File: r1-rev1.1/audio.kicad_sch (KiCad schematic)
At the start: 28 parts, among them J4 HP_3.5mm, J5 LO_3.5mm, Q6 AO3401A, Q7 AO3401A, U9 TLV320AIC3104

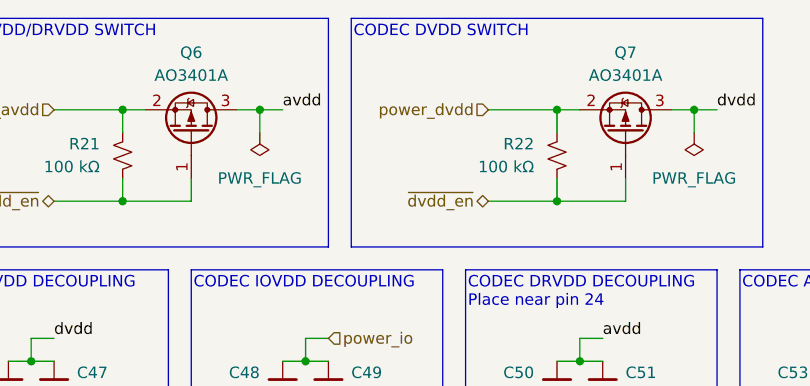
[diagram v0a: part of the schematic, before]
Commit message: Fix symbol library links & resync footprints from KiCAD libraries
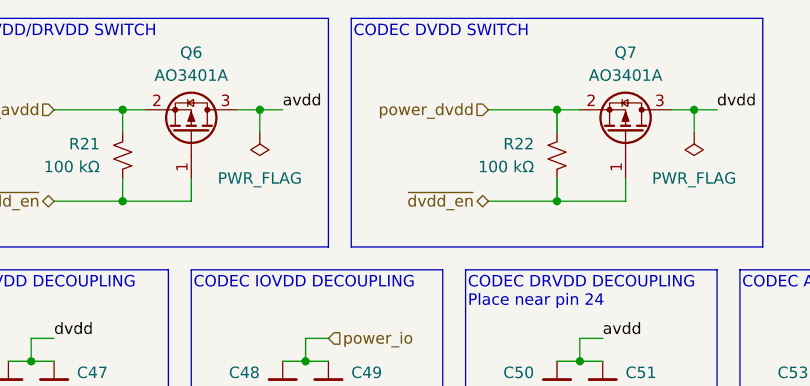
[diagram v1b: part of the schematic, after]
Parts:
- Q6, Q7: symbol Device:Q_PMOS_GSD -> Transistor_FET:Q_PMOS_GSD
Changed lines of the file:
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@@
 	)
 	(symbol
-		(lib_id "Device:Q_PMOS_GSD")
+		(lib_id "Transistor_FET:Q_PMOS_GSD")
 		(at 132.08 27.94 270)
 		(mirror x)
@@
 	)
 	(symbol
-		(lib_id "Device:Q_PMOS_GSD")
+		(lib_id "Transistor_FET:Q_PMOS_GSD")
 		(at 83.82 27.94 270)
 		(mirror x)

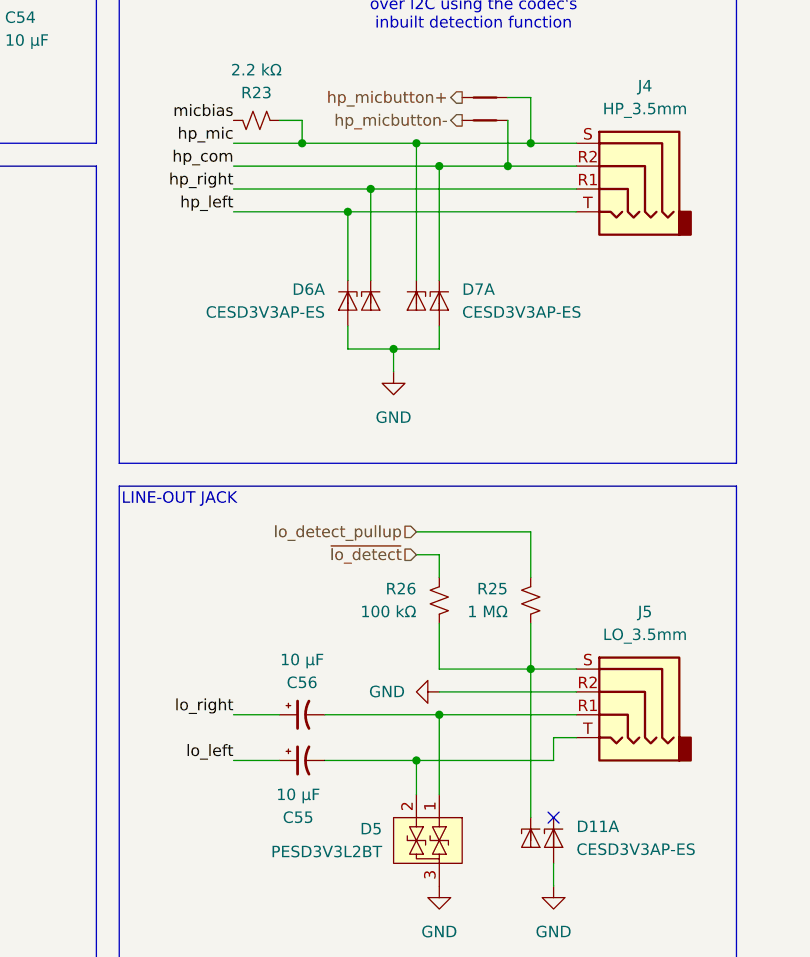
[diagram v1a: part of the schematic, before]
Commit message: Fix incorrect 3.5mm jack pinout
Document the R1-Rev1's wrong pinout properly and fix the pinout
in later revs so that jacks will work properly without needing
a custom adapter.

See Github issue: #12
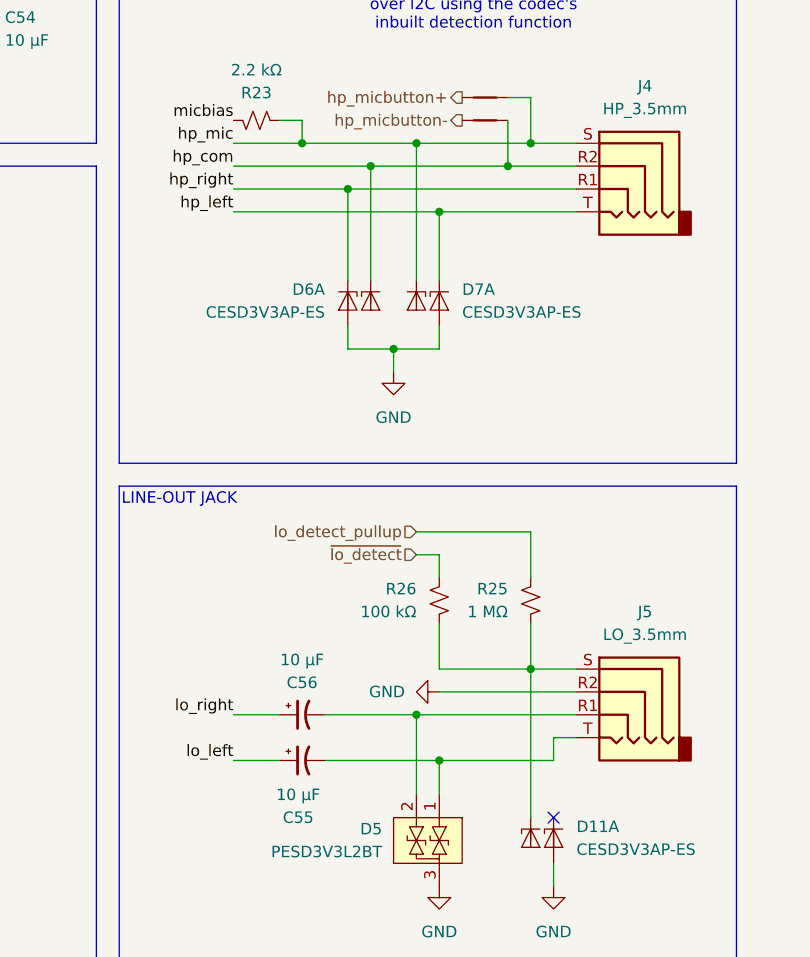
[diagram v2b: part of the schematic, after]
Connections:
- net hp_com: now also D6.2 (K2); no longer D7.1 (K1)
- net hp_left: now also D7.1 (K1); no longer D6.1 (K1)
- net hp_right: now also D6.1 (K1); no longer D6.2 (K2)
- net at C56.2, J5.R1: now also D5.2 (IO2); no longer D5.1 (IO1)
- net at C55.2, J5.T: now also D5.1 (IO1); no longer D5.2 (IO2)
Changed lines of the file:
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@@
+	)
+	(junction
+		(at 210.82 137.16)
+		(diameter 0)
+		(color 0 0 0 0)
 	)
 	(junction
@@
 	)
 	(junction
+		(at 210.82 76.2)
+		(diameter 0)
+		(color 0 0 0 0)
+	)
+	(junction
 		(at 139.7 25.4)
 		(diameter 0)
@@
 	)
 	(junction
+		(at 200.66 73.66)
+		(diameter 0)
+		(color 0 0 0 0)
+	)
+	(junction
 		(at 106.68 91.44)
 		(diameter 0)
@@
 	)
 	(junction
-		(at 210.82 71.12)
-		(diameter 0)
-		(color 0 0 0 0)
-	)
-	(junction
 		(at 134.62 147.32)
 		(diameter 0)
@@
 	)
 	(junction
+		(at 208.28 132.08)
+		(diameter 0)
+		(color 0 0 0 0)
+	)
+	(junction
 		(at 218.44 71.12)
 		(diameter 0)
@@
 	)
 	(junction
-		(at 200.66 76.2)
-		(diameter 0)
-		(color 0 0 0 0)
-	)
-	(junction
 		(at 205.74 91.44)
 		(diameter 0)
@@
 	)
 	(junction
-		(at 203.2 73.66)
-		(diameter 0)
-		(color 0 0 0 0)
-	)
-	(junction
 		(at 127 53.34)
 		(diameter 0)
@@
 	)
 	(junction
-		(at 208.28 137.16)
-		(diameter 0)
-		(color 0 0 0 0)
-	)
-	(junction
-		(at 210.82 132.08)
-		(diameter 0)
-		(color 0 0 0 0)
-	)
-	(junction
 		(at 101.6 157.48)
 		(diameter 0)
@@
 	(junction
 		(at 134.62 144.78)
+		(diameter 0)
+		(color 0 0 0 0)
+	)
+	(junction
+		(at 203.2 71.12)
 		(diameter 0)
 		(color 0 0 0 0)
@@
 	(wire
 		(pts
-			(xy 200.66 76.2) (xy 200.66 83.82)
-		)
-		(stroke
-			(width 0)
-			(type default)
-		)
-	)
-	(wire
-		(pts
 			(xy 106.68 154.94) (xy 106.68 157.48)
 		)
@@
 	(wire
 		(pts
-			(xy 208.28 137.16) (xy 223.52 137.16)
-		)
-		(stroke
-			(width 0)
-			(type default)
-		)
-	)
-	(wire
-		(pts
 			(xy 134.62 144.78) (xy 134.62 147.32)
 		)
@@
 	(wire
 		(pts
-			(xy 210.82 132.08) (xy 226.06 132.08)
+			(xy 198.12 132.08) (xy 208.28 132.08)
 		)
 		(stroke
@@
 	(wire
 		(pts
+			(xy 208.28 132.08) (xy 208.28 140.97)
+		)
+		(stroke
+			(width 0)
+			(type default)
+		)
+	)
+	(wire
+		(pts
 			(xy 134.62 104.14) (xy 134.62 109.22)
 		)
@@
 	(wire
 		(pts
-			(xy 203.2 73.66) (xy 203.2 83.82)
-		)
-		(stroke
-			(width 0)
-			(type default)
-		)
-	)
-	(wire
-		(pts
 			(xy 76.2 35.56) (xy 68.58 35.56)
 		)
@@
 	(wire
 		(pts
-			(xy 203.2 73.66) (xy 226.06 73.66)
-		)
-		(stroke
-			(width 0)
-			(type default)
-		)
-	)
-	(wire
-		(pts
-			(xy 200.66 76.2) (xy 226.06 76.2)
+			(xy 200.66 73.66) (xy 226.06 73.66)
+		)
+		(stroke
+			(width 0)
+			(type default)
+		)
+	)
+	(wire
+		(pts
+			(xy 187.96 76.2) (xy 210.82 76.2)
 		)
 		(stroke
@@
 	(wire
 		(pts
+			(xy 203.2 71.12) (xy 203.2 83.82)
+		)
+		(stroke
+			(width 0)
+			(type default)
+		)
+	)
+	(wire
+		(pts
 			(xy 210.82 88.9) (xy 210.82 91.44)
 		)
@@
 	(wire
 		(pts
-			(xy 208.28 137.16) (xy 208.28 140.97)
-		)
-		(stroke
-			(width 0)
-			(type default)
-		)
-	)
-	(wire
-		(pts
-			(xy 187.96 73.66) (xy 203.2 73.66)
+			(xy 187.96 73.66) (xy 200.66 73.66)
 		)
 		(stroke
@@
 	(wire
 		(pts
-			(xy 210.82 71.12) (xy 218.44 71.12)
+			(xy 187.96 71.12) (xy 203.2 71.12)
 		)
 		(stroke
@@
 	(wire
 		(pts
+			(xy 208.28 132.08) (xy 226.06 132.08)
+		)
+		(stroke
+			(width 0)
+			(type default)
+		)
+	)
+	(wire
+		(pts
 			(xy 223.52 137.16) (xy 223.52 134.62)
 		)
@@
 	(wire
 		(pts
+			(xy 210.82 76.2) (xy 210.82 83.82)
+		)
+		(stroke
+			(width 0)
+			(type default)
+		)
+	)
+	(wire
+		(pts
 			(xy 63.5 53.34) (xy 66.04 53.34)
 		)
@@
 		)
 	)
+	(wire
+		(pts
+			(xy 200.66 73.66) (xy 200.66 83.82)
+		)
+		(stroke
+			(width 0)
+			(type default)
+		)
+	)
 	(bus
 		(pts
@@
 	(wire
 		(pts
-			(xy 187.96 71.12) (xy 210.82 71.12)
-		)
-		(stroke
-			(width 0)
-			(type default)
-		)
-	)
-	(wire
-		(pts
 			(xy 132.08 139.7) (xy 134.62 139.7)
 		)
@@
 	(wire
 		(pts
-			(xy 198.12 137.16) (xy 208.28 137.16)
+			(xy 198.12 137.16) (xy 210.82 137.16)
 		)
 		(stroke
@@
 	(wire
 		(pts
-			(xy 210.82 71.12) (xy 210.82 83.82)
-		)
-		(stroke
-			(width 0)
-			(type default)
-		)
-	)
-	(wire
-		(pts
 			(xy 106.68 157.48) (xy 104.14 157.48)
 		)
@@
 	(wire
 		(pts
+			(xy 203.2 71.12) (xy 218.44 71.12)
+		)
+		(stroke
+			(width 0)
+			(type default)
+		)
+	)
+	(wire
+		(pts
 			(xy 60.96 104.14) (xy 76.2 104.14)
 		)
@@
 	(wire
 		(pts
+			(xy 210.82 137.16) (xy 210.82 140.97)
+		)
+		(stroke
+			(width 0)
+			(type default)
+		)
+	)
+	(wire
+		(pts
 			(xy 220.98 127) (xy 220.98 143.51)
 		)
@@
 	(wire
 		(pts
-			(xy 187.96 76.2) (xy 200.66 76.2)
-		)
-		(stroke
-			(width 0)
-			(type default)
-		)
-	)
-	(wire
-		(pts
 			(xy 66.04 58.42) (xy 68.58 58.42)
 		)
@@
 	(wire
 		(pts
-			(xy 198.12 132.08) (xy 210.82 132.08)
-		)
-		(stroke
-			(width 0)
-			(type default)
-		)
-	)
-	(wire
-		(pts
 			(xy 66.04 50.8) (xy 66.04 53.34)
 		)
@@
 	(wire
 		(pts
-			(xy 210.82 132.08) (xy 210.82 140.97)
+			(xy 210.82 137.16) (xy 223.52 137.16)
 		)
 		(stroke
@@
 		)
 		(stroke
+			(width 0)
+			(type default)
+		)
+	)
+	(wire
+		(pts
+			(xy 210.82 76.2) (xy 226.06 76.2)
+		)
+		(stroke
